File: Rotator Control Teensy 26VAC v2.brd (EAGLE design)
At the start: 88.9 x 76.2 mm, 61 parts, among them K4 G5LE, K5 G5LE, K6 G5LE, Q1 BSS123, Q2 BSS123, Q3 BSS123

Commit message: add 5V LED, polishing
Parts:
- removed 12VDC, 36VDC, BRAKE, DIR, MOTOR: (no value), led:LED3MM
- removed R102: 1200, rcl:R0805
- added LED1: Motor, led:LED3MM
- added LED2: Dir, led:LED3MM
- added LED3: Brake, led:LED3MM
- added LED4: 36V, led:LED3MM
- added LED5: 12V, led:LED3MM
- added LED6: 5V, led:LED3MM
- added R18: 500, rcl:R0805
- added R21: 1200, rcl:R0805
- C19: value (none) -> 100u
- C2: device rcl:E7,5-18 -> rcl:EB22,5D
- D4, D5, D6: value (none) -> 1N4148
- X1: value (none) -> Rotor
- X2: value (none) -> 26VAC
- moved R101 20.5 mm to (52.1, 59.7)
- moved D1 3.81 mm to (78.7, 49.5)
- moved X2 3.81 mm to (78.7, 43.2)
- moved C10 3.81 mm to (73.7, 44.5)
- moved C2 3.59 mm to (66.7, 56.5)
- moved Q1 2.84 mm to (29.2, 54.6), turned to 270 degrees
- moved Q2 2.54 mm to (29.2, 36.8), turned to 270 degrees
- moved Q3 2.54 mm to (29.2, 19.1), turned to 270 degrees
- moved C11 1.27 mm to (45.1, 59.1)
- moved C12 1.27 mm to (40.0, 59.1)
- moved U$2 1.27 mm to (42.5, 61.6)
- renumbered K4 to K1, K5 to K2, K6 to K3, R103 to R19, R104 to R20, U$3 to C19
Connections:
- net N$19 renamed CAP2
- net N$2 renamed N/C
- removed net +5V: U$1.VIN
- new net +12V1: R18.2, U$1.VIN
- new net N$2: LED6.A, R18.1
- net +12V: now also R21.2; no longer R102.2
- net +3V3: no longer U$1.3V3_LO
- net GND: now also LED4.K, LED5.K, LED6.K; no longer 12VDC.K, 36VDC.K
- net LEFT: now also C4.1, K2.O, R6.1, X1.6; no longer C3.1, K2.S, R5.1, X1.5
- net N$10: now also LED2.K; no longer DIR.K
- net N$11: now also LED3.K; no longer BRAKE.K
- net N$15: now also LED4.A; no longer 36VDC.A
- net N$16: now also LED5.A, R21.1; no longer 12VDC.A, R102.1
- net N$4: now also LED1.A; no longer MOTOR.A
- net N$5: now also LED2.A; no longer DIR.A
- net N$6: now also LED3.A; no longer BRAKE.A
- net N$9: now also LED1.K; no longer MOTOR.K
- net RIGHT: now also C3.1, K2.S, R5.1, X1.5; no longer C4.1, K2.O, R6.1, X1.6
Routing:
- net RIGHT: track 47.7 -> 38.4 mm
- net LEFT: track 38.4 -> 47.7 mm
- net N$11: track 21.7 -> 13.5 mm
- net N$10: track 21.6 -> 13.7 mm
- net +12V1: track 0.00 -> 7.46 mm
- net N$9: track 18.1 -> 13.7 mm
- net 36VDC: track 55.9 -> 52.3 mm
- net N$2: track 0.00 -> 2.93 mm
- net +12V: track 110.3 -> 107.4 mm
- net N$12: track 20.4 -> 17.7 mm
- net N$5: track 2.67 -> 5.21 mm
- net N$6: track 2.49 -> 5.03 mm
- net N$16: track 5.29 -> 2.93 mm
- net N$15: track 4.76 -> 2.93 mm
- net N$4: track 3.57 -> 4.84 mm
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
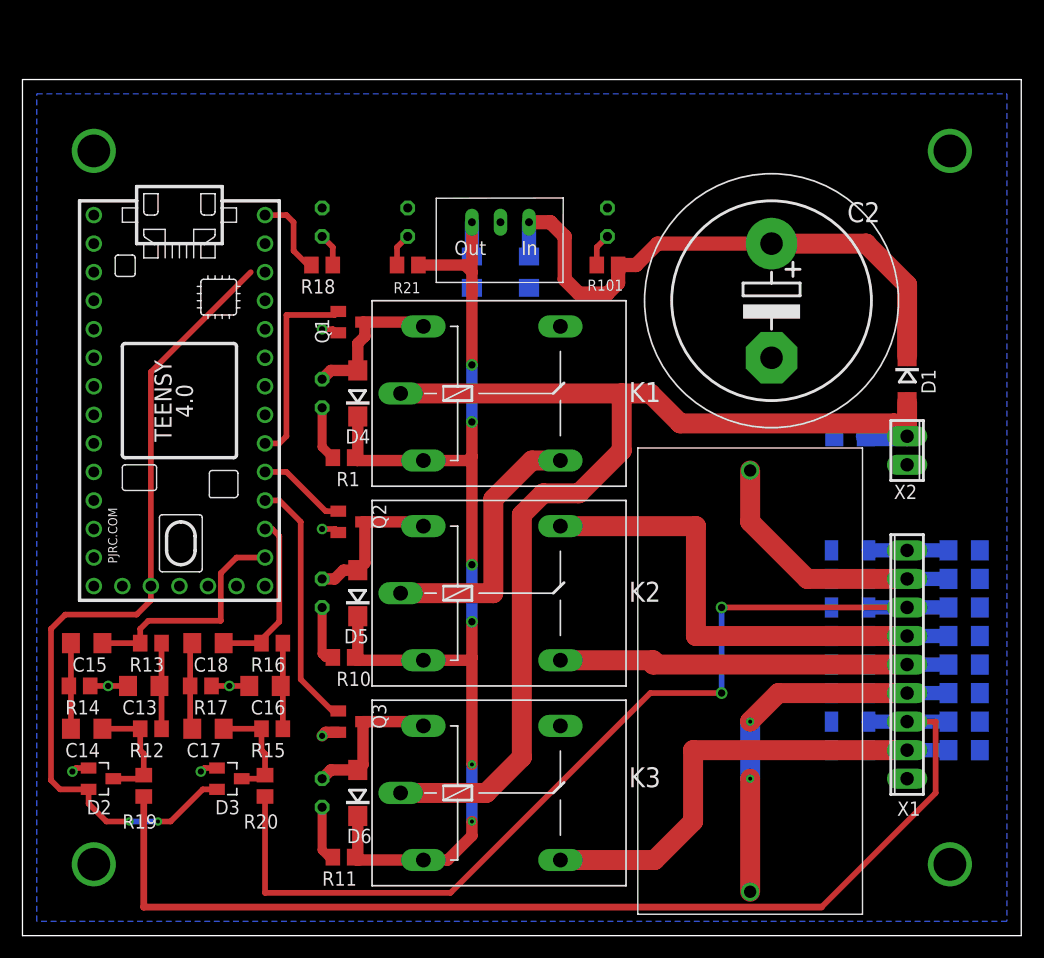
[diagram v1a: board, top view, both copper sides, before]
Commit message: Simplified by running relays from 5V from USB 26V AC is only for the rotator
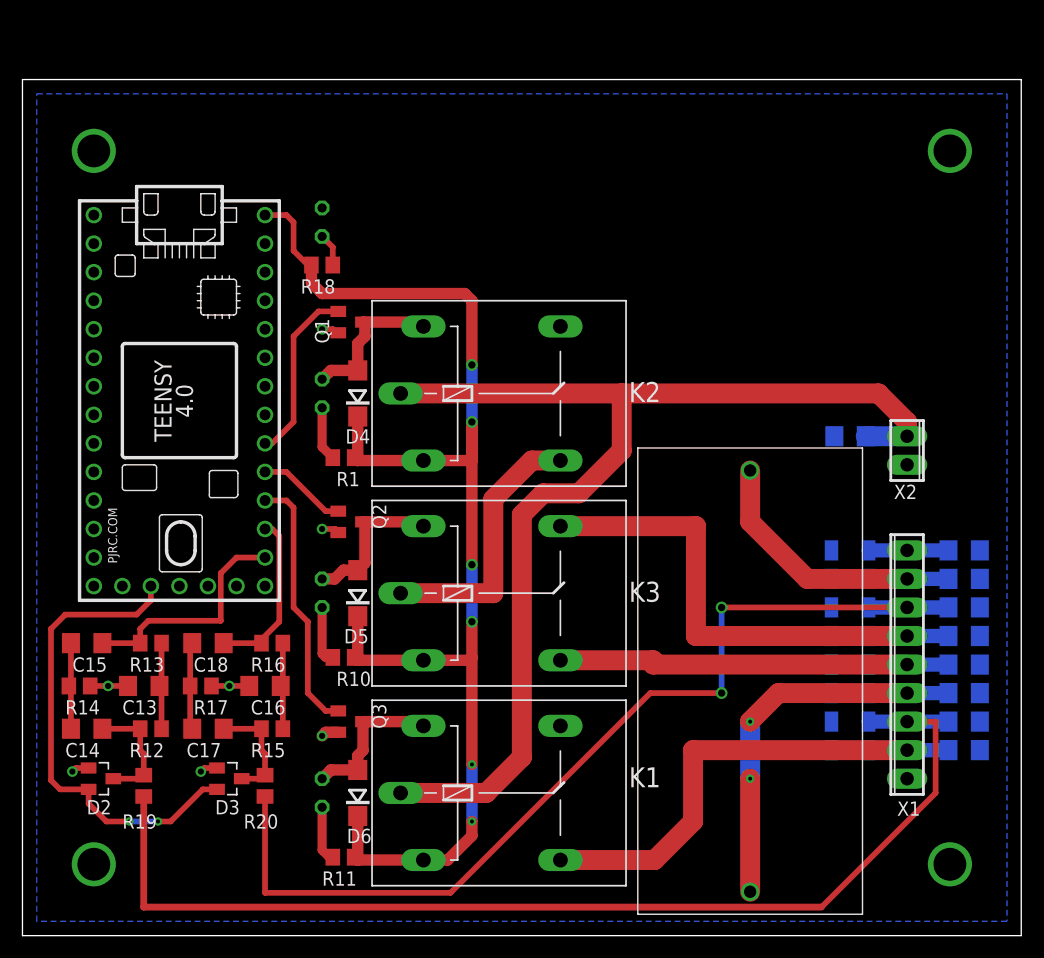
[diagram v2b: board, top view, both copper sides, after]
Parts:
- removed C11, C12: .1, rcl:C1206
- removed C2: 4700, rcl:EB22,5D
- removed D1: 1N4148, diode:DO214AC
- removed LED4: 36V, led:LED3MM
- removed LED5: 12V, led:LED3MM
- removed R101: 3600, rcl:R0805
- removed R21: 1200, rcl:R0805
- removed U$2: VX78012-500, my-library:DC2DC_SIP3
- R1, R10, R11: value 1200 -> 560
- R18: value 500 -> 560
- moved K1 35.6 mm to (43.2, 12.7)
- moved K3 17.8 mm to (43.2, 30.5)
- moved K2 17.8 mm to (43.2, 48.3)
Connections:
- removed net +12V: C12.1, D4.C, D5.C, D6.C, K1.1, K2.1, K3.1, R1.2, R10.2, R11.2, R21.2, U$2.P$3
- removed net +12V1: R18.2, U$1.VIN
- removed net 36VDC: C11.1, C2.+, D1.C, R101.2, U$2.P$1
- removed net N$15: LED4.A, R101.1
- removed net N$16: LED5.A, R21.1
- new net +5V: D4.C, D5.C, D6.C, K1.1, K2.1, K3.1, R1.2, R10.2, R11.2, R18.2, U$1.VIN
- net 26VAC: now also K2.P; no longer D1.A, K3.P
- net BRAKE: now also K1.S; no longer K3.S
- net GND: no longer C11.2, C12.2, C2.-, LED4.K, LED5.K, U$2.P$2
- net LEFT: now also K3.O; no longer K2.O
- net N$10: now also K3.2; no longer K2.2
- net N$11: now also K1.2; no longer K3.2
- net N$8: now also K2.S, K3.P; no longer K1.S, K2.P
- net N$9: now also K2.2; no longer K1.2
- net RIGHT: now also K3.S; no longer K2.S
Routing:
- net +5V: track 0.00 -> 119.6 mm, vias 0 -> 6
- net +12V: track 107.4 -> 0.00 mm, vias 6 -> 0
- net 36VDC: track 52.3 -> 0.00 mm
- net +3V3: track 74.5 -> 42.9 mm
- net +12V1: track 7.46 -> 0.00 mm
- net N$15: track 2.93 -> 0.00 mm
- net N$16: track 2.93 -> 0.00 mm
- net 26VAC: track 103.4 -> 101.1 mm
- net N$13: track 17.7 -> 15.8 mm
- net N$12: track 22.5 -> 23.2 mm

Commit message: switched LED to -.28 inch 4 digit plus driver with keyswitch capability
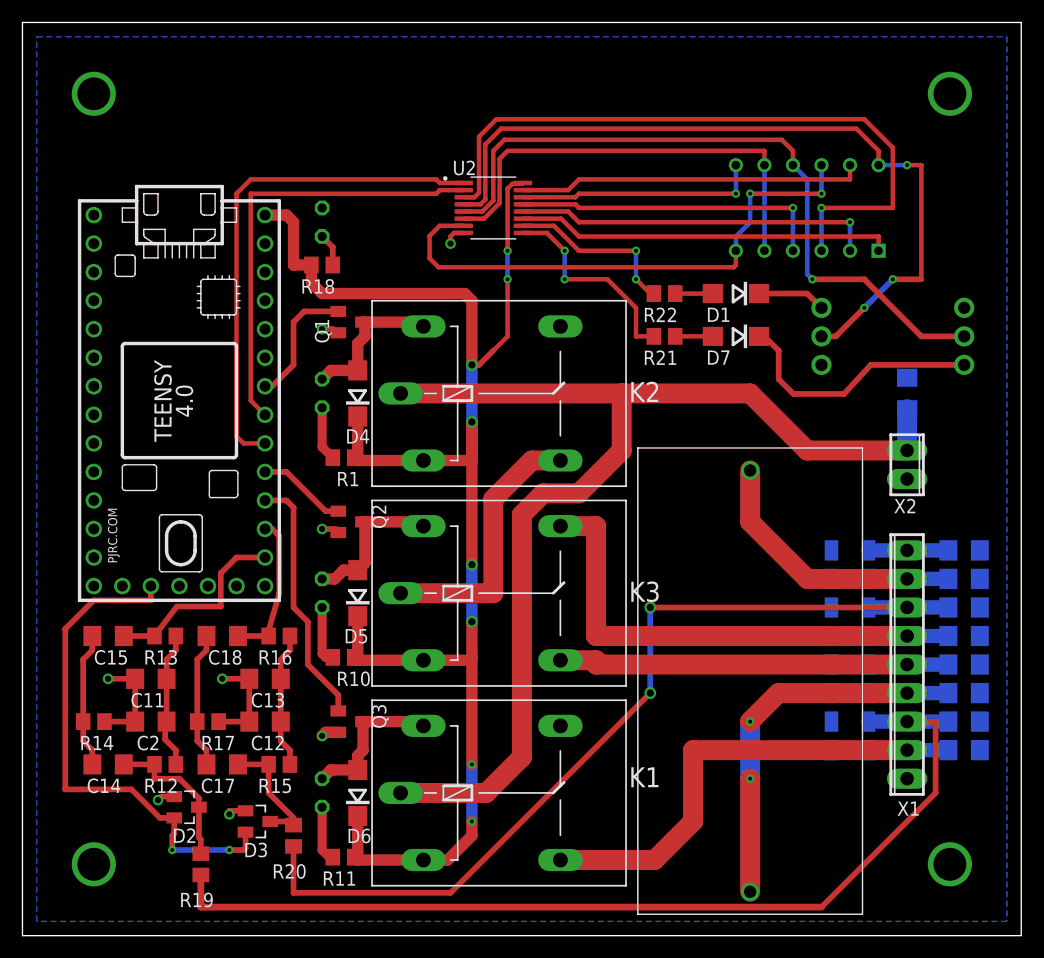
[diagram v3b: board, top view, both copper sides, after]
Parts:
- removed C16: .22, rcl:C1206
- added C11, C12, C2: .1, rcl:C1206
- added D1, D7: 1N4148, diode:DO214AC
- added LED5: LDQ-M284RI, my-library:LDQ-M284RI_LUM
- added R21, R22: 39K, rcl:R0805
- added U1, U3: SWITCH_TP_1825097-1, my-library:SW3-TOGGLE-2POL_P100
- added U2: MAX6959BAEE+, MAX6959BAEE_:SOP63P602X175-16N
- C13: value .22 -> .1
- moved C13 10.8 mm to (21.6, 22.9)
- moved R19 8.64 mm to (15.9, 6.35)
- moved D2 8.03 mm to (14.6, 11.4)
- moved C10 6.35 mm to (78.7, 48.3), turned to 90 degrees
- moved R20 5.12 mm to (24.1, 8.89)
- moved D3 4.58 mm to (21.0, 10.2)
- moved C14 3.70 mm to (7.62, 15.2)
- moved R14 3.42 mm to (6.35, 19.1)
- moved C17 3.42 mm to (17.8, 15.2)
- moved R12 3.42 mm to (12.7, 15.2)
- moved R17 3.24 mm to (16.5, 19.1)
- moved R15 3.24 mm to (22.9, 15.2)
- moved C15 2.01 mm to (7.62, 26.7)
- moved C18 1.42 mm to (17.8, 26.7)
- moved R13 1.42 mm to (12.7, 26.7)
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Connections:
- new net DIG0: LED5.12, U1.2, U2.4
- new net DIG1: LED5.9, U2.5, U3.2
- new net DIG2: LED5.5, LED5.8, U2.6
- new net DIG3: LED5.10, LED5.6, U2.7
- new net N$15: R21.1, U2.9
- new net N$16: R22.1, U2.10
- new net N$19: D7.A, R21.2
- new net N$20: D1.A, R22.2
- new net N$24: D1.C, U1.3
- new net N$25: D7.C, U3.3
- new net SCL0: U$1.19/A5/SCL, U2.2
- new net SDA0: U$1.18/A4/SDA, U2.1
- new net SEG4: LED5.1, U2.11
- new net SEG5: LED5.2, U2.12
- new net SEG6: LED5.4, U2.13
- new net SEG7: LED5.7, U2.14
- new net SEG8: LED5.11, U2.15
- new net SEG9: LED5.3, U2.3
- net +5V: now also U2.16
- net GND: now also C11.2, C12.2, C2.2, U2.8; no longer C16.2
- net N$13: now also U$1.20/A6; no longer U$1.18/A4/SDA
- net N$17: now also C11.1, C2.1; no longer C13.1
- net N$21: now also C12.1, C13.1; no longer C16.1
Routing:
- net DIG0: track 0.00 -> 69.6 mm, vias 0 -> 3
- net DIG1: track 0.00 -> 62.7 mm, vias 0 -> 1
- net SEG9: track 0.00 -> 60.6 mm, vias 0 -> 1
- net DIG3: track 0.00 -> 48.8 mm, vias 0 -> 2
- net SDA0: track 0.00 -> 45.3 mm
- net DIG2: track 0.00 -> 40.5 mm
- net SCL0: track 0.00 -> 39.3 mm
- net SEG4: track 0.00 -> 33.6 mm
- net SEG5: track 0.00 -> 32.0 mm, vias 0 -> 1
- net SEG8: track 0.00 -> 30.8 mm
- net SEG6: track 0.00 -> 28.0 mm, vias 0 -> 1
- net N$25: track 0.00 -> 23.0 mm
- net SEG7: track 0.00 -> 21.6 mm, vias 0 -> 1
- net +5V: track 119.6 -> 139.3 mm, vias 6 -> 8
- net N$15: track 0.00 -> 18.4 mm, vias 0 -> 2
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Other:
- board size 88.9 x 76.2 mm -> 88.9 x 81.3 mm
- board text added: "WA1HCO (C) 2022 Creative Commons Lic, V4 Share Alike"

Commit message: Released this version to OshPark for fab
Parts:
- removed D7: 1N4148, diode:DO214AC
- removed R5, R6, R8, R9: VARISTORCN1206, varistor:CT/CN1206
- removed U1, U3: SWITCH_TP_1825097-1, my-library:SW3-TOGGLE-2POL_P100
- added C16: .1, rcl:C1206
- added LED4: 26VAC, led:LED3MM
- added U$2, U$3: SWITCH_AEXIT_6X6X9.5, my-library:PUSHBUTTON_6X6
- D1, D4, D5, D6: device diode:DO214AC -> adafruit:SOD-123
- R4: value VARISTORCN1206 -> 3600; device varistor:CT/CN1206 -> rcl:R0805
- moved R4 55.7 mm to (33.0, 59.7), flipped to the top
- moved R2 28.5 mm to (83.8, 43.2), turned to 180 degrees
- moved D1 25.5 mm to (38.1, 59.7), turned to 0 degrees
- moved C1 10.2 mm to (73.7, 16.5), turned to 0 degrees
- moved C3 10.2 mm to (73.7, 24.1), turned to 0 degrees
- moved C4 10.2 mm to (73.7, 26.7), turned to 0 degrees
- moved C5 10.2 mm to (73.7, 34.3), turned to 0 degrees
- moved C6 10.2 mm to (73.7, 29.2), turned to 0 degrees
- moved C7 10.2 mm to (73.7, 19.1), turned to 0 degrees
- moved C8 10.2 mm to (73.7, 21.6), turned to 0 degrees
- moved C9 10.2 mm to (73.7, 31.8), turned to 0 degrees
- moved R3 10.2 mm to (83.8, 19.1), turned to 180 degrees
- moved R7 10.2 mm to (83.8, 29.2), turned to 180 degrees
- moved C10 7.18 mm to (73.7, 43.2), turned to 0 degrees
- moved R21 5.24 mm to (58.4, 48.3)
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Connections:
- net +5V: now also C16.1
- net 26VAC: now also D1.A, R2.1
- net BRAKE: no longer R2.1
- net CAP1: no longer R4.1
- net CAP2: no longer R8.1
- net DIG0: now also U$2.P$1, U$3.P$1; no longer U1.2
- net DIG1: no longer U3.2
- net GND: now also C16.2, LED4.K; no longer R4.2, R5.2, R6.2, R8.2, R9.2
- net LEFT: no longer R6.1
- net N$19: now also U$3.P$2; no longer D7.A
- net N$20: now also U$2.P$2; no longer D1.A
- net N$24: now also R4.2; no longer U1.3
- net N$25: now also LED4.A, R4.1; no longer D7.C, U3.3
- net N/C: no longer R9.1
- net RIGHT: no longer R5.1
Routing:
- net DIG1: track 62.7 -> 36.0 mm, vias 1 -> 0
- net N$20: track 3.35 -> 23.7 mm
- net N$25: track 23.0 -> 2.93 mm
- net DIG0: track 69.6 -> 83.7 mm, vias 3 -> 1
- net 26VAC: track 100.9 -> 114.0 mm
- net +3V3: track 45.9 -> 33.6 mm
- net +5V: track 139.3 -> 149.4 mm, vias 8 -> 2
- net DIG3: track 48.8 -> 41.3 mm
- net N$16: track 15.6 -> 20.5 mm
- net N$15: track 18.4 -> 22.8 mm
- net GND: track 28.4 -> 32.5 mm, vias 12 -> 13
- net N$24: track 6.10 -> 2.28 mm
- net N$12: track 22.6 -> 26.2 mm, vias 0 -> 3
- net CAP1: track 37.3 -> 33.7 mm
- net RIGHT: track 38.4 -> 34.9 mm
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
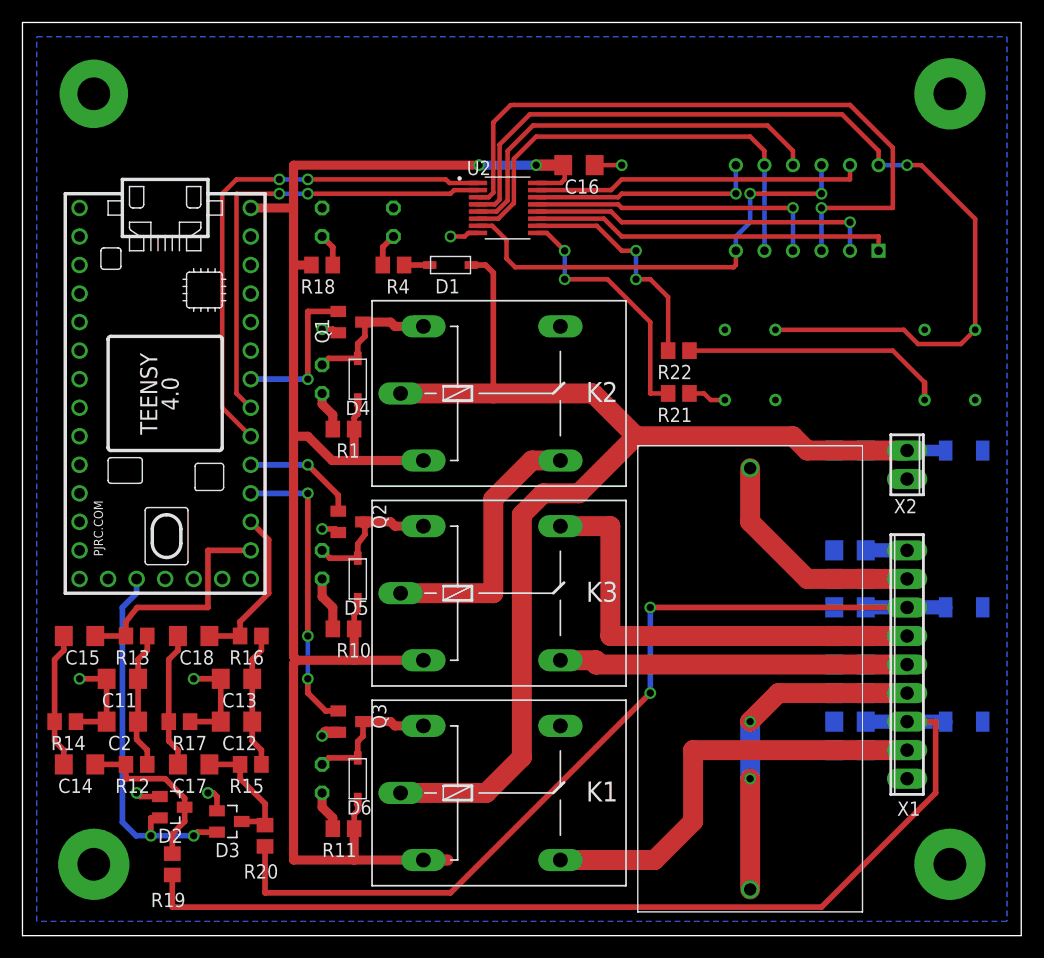
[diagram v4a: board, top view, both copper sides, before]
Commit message: Add 5V power supply resistors to the rotor pot leads
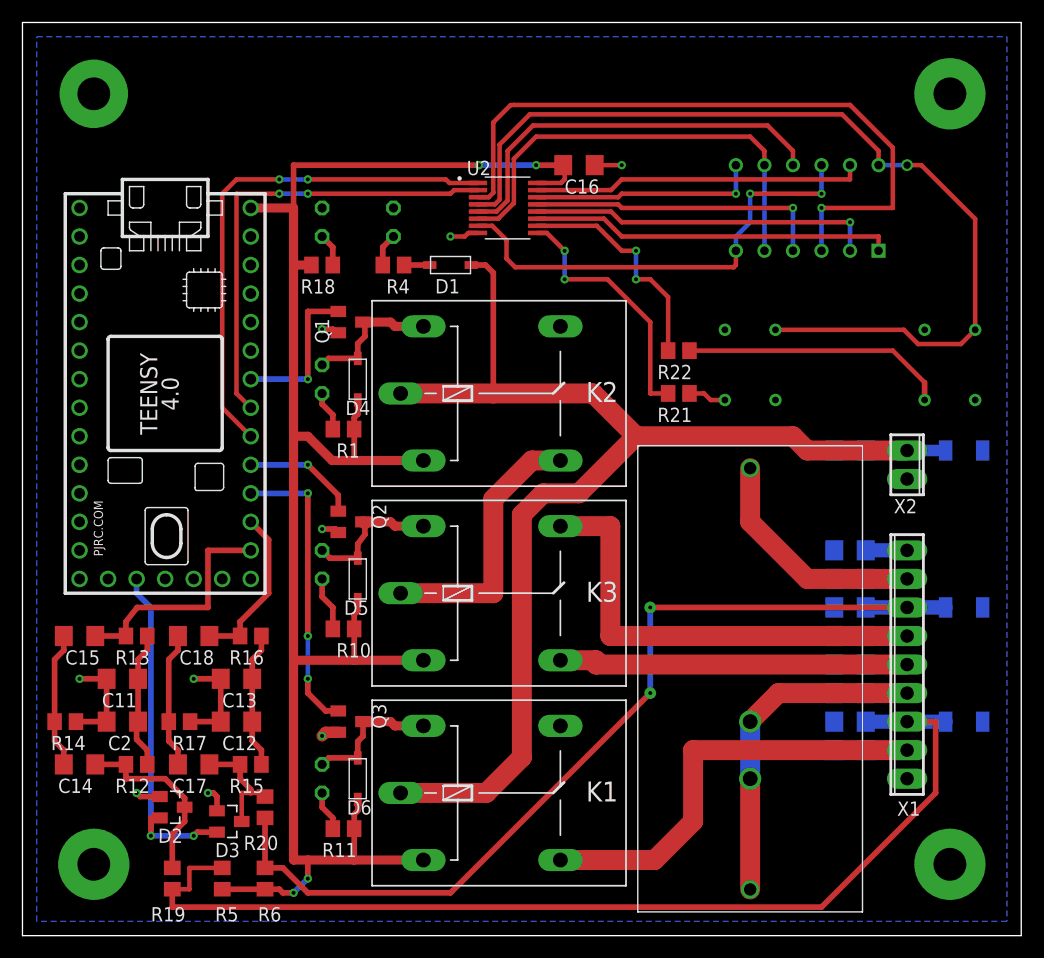
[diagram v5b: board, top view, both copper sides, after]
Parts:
- added R5, R6: 360, rcl:R0805
- moved R20 2.54 mm to (21.6, 11.4)
- moved R19 1.27 mm to (13.3, 5.08)
- renumbered R2 to Z1, R3 to Z3, R7 to Z2
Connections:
- net +5V: now also R5.2, R6.2
- net WIPER+: now also R5.1
- net WIPER-: now also R6.1
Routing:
- net +5V: track 149.4 -> 157.2 mm, vias 2 -> 4
- net WIPER+: track 91.0 -> 96.1 mm
- net +3V3: track 33.6 -> 31.8 mm
- net N$3: track 15.3 -> 16.6 mm
- net WIPER-: track 83.4 -> 84.6 mm
- net N$1: track 11.4 -> 10.6 mm
- net GND: track 32.5 -> 32.0 mm
